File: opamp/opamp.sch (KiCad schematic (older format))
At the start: 7 parts, among them CON1 BARREL_JACK, CON2 BARREL_JACK, P1 PWR_IN, U1 OPAMP

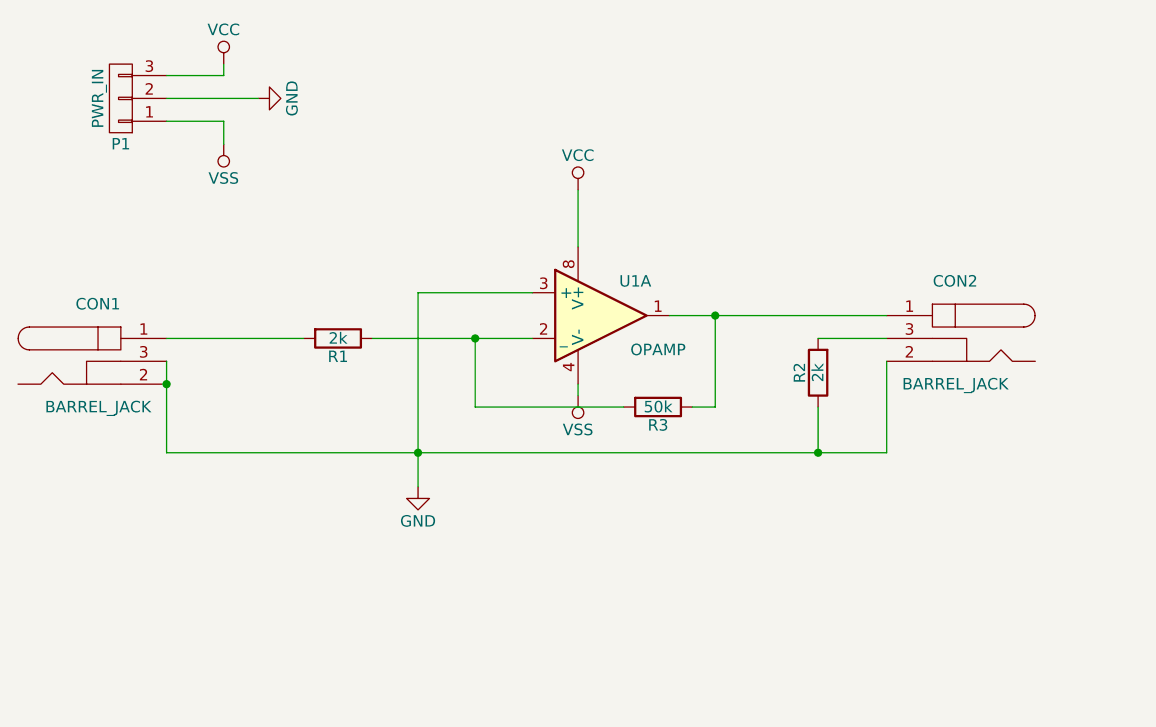
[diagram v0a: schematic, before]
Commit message: Added Simulation Circuits and POV board
Added a BJT characteristics simulation circuit
Add a Voltage Divider simulation circuit
Add an amplifier simulation circuit
Add a Nokia LCD breakout board
Add a POV LED MKL05Z board
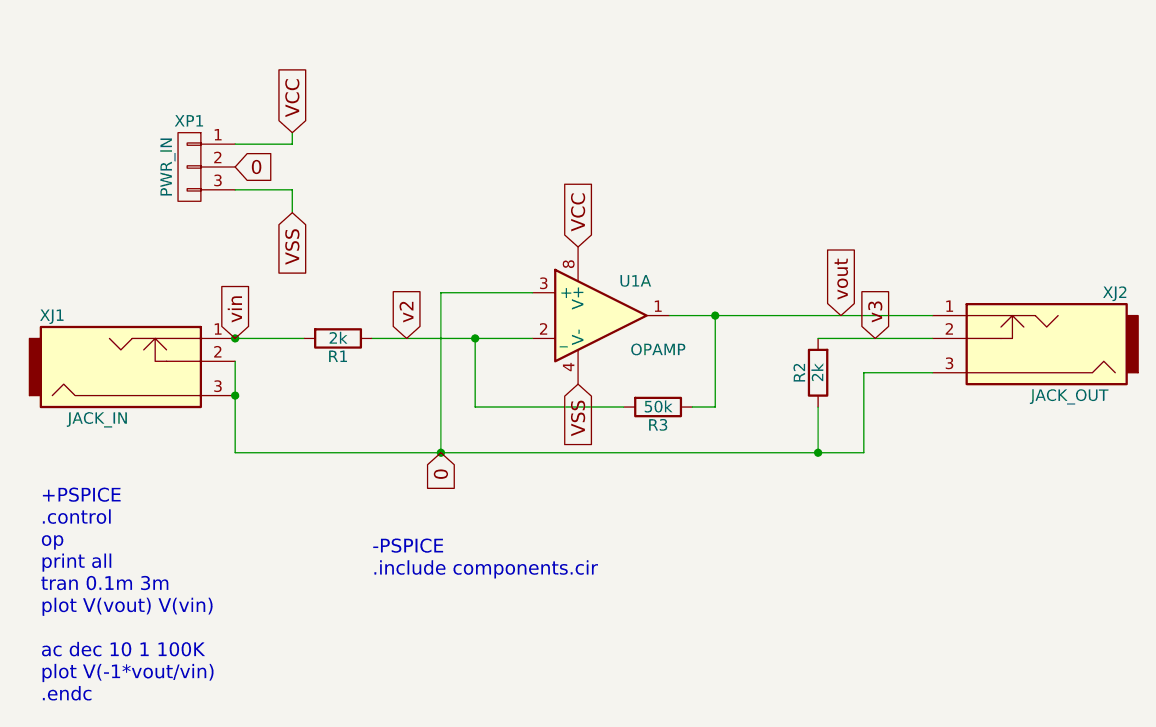
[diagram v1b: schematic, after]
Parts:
- removed CON1, CON2: BARREL_JACK, symbol BARREL_JACK
- added XJ1: JACK_IN, symbol JACK_2P
- added XJ2: JACK_OUT, symbol JACK_2P
- renumbered P1 to XP1
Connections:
- net VCC: now also XP1.1 (P1); no longer XP1.3 (P3)
- net VSS: now also XP1.3 (P3); no longer XP1.1 (P1)
- net v2: now reaches R1.1, R3.2, U1.2 (_)
- net vin: now reaches R1.2
- net vin: now also XJ1.1
- net v3: now reaches R2.2
- net v3: now also XJ2.2
- net vout: now reaches R3.1, U1.1
- net vout: now also XJ2.1
- net GND renamed 0
- net 0: now also XJ1.2, XJ1.3, XJ2.3
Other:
- note added: "+PSPICE\n.control\nop\nprint all\ntran 0.1m 3m\nplot V(vout) V(vin)\n\nac dec 10 1 100K\nplot V(-1*vout/vin)\n.endc"
- note added: "-PSPICE\n.include components.cir"
- moved on the sheet: XP1
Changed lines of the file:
@@
-$EndComp
-$Comp
-L VSS #PWR01
-U 1 1 57F76045
-P 5400 3200
-F 0 "#PWR01" H 5400 3050 50  0001 C CNN
-F 1 "VSS" H 5400 3350 50  0000 C CNN
-F 2 "" H 5400 3200 50  0000 C CNN
-F 3 "" H 5400 3200 50  0000 C CNN
-	1    5400 3200
-	-1   0    0    1
-$EndComp
-$Comp
-L BARREL_JACK CON1
-U 1 1 57F76321
-P 3300 3050
-F 0 "CON1" H 3300 3300 50  0000 C CNN
-F 1 "BARREL_JACK" H 3300 2850 50  0000 C CNN
-F 2 "" H 3300 3050 50  0000 C CNN
-F 3 "" H 3300 3050 50  0000 C CNN
-	1    3300 3050
-	1    0    0    -1
-$EndComp
-$Comp
-L BARREL_JACK CON2
-U 1 1 57F7634E
-P 7050 2950
-F 0 "CON2" H 7050 3200 50  0000 C CNN
-F 1 "BARREL_JACK" H 7050 2750 50  0000 C CNN
-F 2 "" H 7050 2950 50  0000 C CNN
-F 3 "" H 7050 2950 50  0000 C CNN
-	1    7050 2950
-	-1   0    0    -1
 $EndComp
 $Comp
@@
 $EndComp
 $Comp
-L GND #PWR02
-U 1 1 57F7696D
-P 4700 3600
-F 0 "#PWR02" H 4700 3350 50  0001 C CNN
-F 1 "GND" H 4700 3450 50  0000 C CNN
-F 2 "" H 4700 3600 50  0000 C CNN
-F 3 "" H 4700 3600 50  0000 C CNN
-	1    4700 3600
+L CONN_01X03 XP1
+U 1 1 57F76C49
+P 3700 2200
+F 0 "XP1" H 3700 2400 50  0000 C CNN
+F 1 "PWR_IN" V 3800 2200 50  0000 C CNN
+F 2 "" H 3700 2200 50  0000 C CNN
+F 3 "" H 3700 2200 50  0000 C CNN
+	1    3700 2200
+	-1   0    0    -1
+$EndComp
+$Comp
+L LM193 U1
+U 1 1 5820773C
+P 5500 2850
+F 0 "U1" H 5650 3000 50  0000 C CNN
+F 1 "OPAMP" H 5750 2700 50  0000 C CNN
+F 2 "" H 5500 2850 50  0000 C CNN
+F 3 "" H 5500 2850 50  0000 C CNN
+	1    5500 2850
 	1    0    0    -1
 $EndComp
+Text GLabel 4800 3450 3    60   Input ~ 0
+0
+Text GLabel 5400 3150 3    60   Input ~ 0
+VSS
+Text GLabel 4150 2400 3    60   Input ~ 0
+VSS
+Text Notes 3050 4550 0    60   ~ 0
++PSPICE\n.control\nop\nprint all\ntran 0.1m 3m\nplot V(vout) V(vin)\n\nac dec 10 1 100K\nplot V(-1*vout/vin)\n.endc
+Text GLabel 3900 2950 1    60   Input ~ 0
+vin
+Text GLabel 6550 2850 1    60   Input ~ 0
+vout
+Text GLabel 4650 2950 1    60   Input ~ 0
+v2
+Text GLabel 6700 2950 1    60   Input ~ 0
+v3
+Text GLabel 3900 2200 2    60   Input ~ 0
+0
 $Comp
-L CONN_01X03 P1
-U 1 1 57F76C49
-P 3400 1900
-F 0 "P1" H 3400 2100 50  0000 C CNN
-F 1 "PWR_IN" V 3500 1900 50  0000 C CNN
-F 2 "" H 3400 1900 50  0000 C CNN
-F 3 "" H 3400 1900 50  0000 C CNN
-	1    3400 1900
+L JACK_2P XJ1
+U 1 1 59346446
+P 3450 3050
+F 0 "XJ1" H 3100 2850 50  0000 C CNN
+F 1 "JACK_IN" H 3300 3300 50  0000 C CNN
+F 2 "" H 3450 3050 50  0001 C CNN
+F 3 "" H 3450 3050 50  0001 C CNN
+	1    3450 3050
+	1    0    0    1
+$EndComp
+$Comp
+L JACK_2P XJ2
+U 1 1 59346830
+P 7400 2950
+F 0 "XJ2" H 7050 2750 50  0000 C CNN
+F 1 "JACK_OUT" H 7250 3200 50  0000 C CNN
+F 2 "" H 7400 2950 50  0001 C CNN
+F 3 "" H 7400 2950 50  0001 C CNN
+	1    7400 2950
 	-1   0    0    1
 $EndComp
-$Comp
-L VCC #PWR03
-U 1 1 57F76CA4
-P 3850 1750
-F 0 "#PWR03" H 3850 1600 50  0001 C CNN
-F 1 "VCC" H 3850 1900 50  0000 C CNN
-F 2 "" H 3850 1750 50  0000 C CNN
-F 3 "" H 3850 1750 50  0000 C CNN
-	1    3850 1750
-	1    0    0    -1
-$EndComp
-$Comp
-L VSS #PWR04
-U 1 1 57F76CC6
-P 3850 2100
-F 0 "#PWR04" H 3850 1950 50  0001 C CNN
-F 1 "VSS" H 3850 2250 50  0000 C CNN
-F 2 "" H 3850 2100 50  0000 C CNN
-F 3 "" H 3850 2100 50  0000 C CNN
-	1    3850 2100
-	-1   0    0    1
-$EndComp
-$Comp
-L GND #PWR05
-U 1 1 57F76CE8
-P 4000 1900
-F 0 "#PWR05" H 4000 1650 50  0001 C CNN
-F 1 "GND" H 4000 1750 50  0000 C CNN
-F 2 "" H 4000 1900 50  0000 C CNN
-F 3 "" H 4000 1900 50  0000 C CNN
-	1    4000 1900
-	0    -1   -1   0
-$EndComp
-Wire Wire Line
-	5400 3150 5400 3200
-Wire Wire Line
-	3600 2950 4200 2950
 Wire Wire Line
 	4500 2950 5200 2950
 Wire Wire Line
-	5800 2850 6750 2850
+	5800 2850 6950 2850
 Wire Wire Line
-	6750 2950 6450 2950
-Wire Wire Line
-	6750 3450 6750 3050
-Wire Wire Line
-	3600 3450 6750 3450
+	6450 2950 6950 2950
 Wire Wire Line
 	6450 3450 6450 3250
-Wire Wire Line
-	3600 3050 3600 3450
-Connection ~ 6450 3450
-Connection ~ 3600 3150
 Wire Wire Line
 	5900 3250 6000 3250
@@
 Connection ~ 4950 2950
 Wire Wire Line
-	4700 2750 4700 3600
-Connection ~ 4700 3450
+	4150 2050 4150 2100
 Wire Wire Line
-	5200 2750 4700 2750
+	4150 2100 3900 2100
 Wire Wire Line
-	3850 1750 3850 1800
+	4150 2400 4150 2300
 Wire Wire Line
-	3850 1800 3600 1800
+	4150 2300 3900 2300
 Wire Wire Line
-	3600 1900 4000 1900
+	4800 3450 4800 2750
 Wire Wire Line
-	3850 2100 3850 2000
+	4800 2750 5200 2750
 Wire Wire Line
-	3850 2000 3600 2000
-$Comp
-L LM193 U1
-U 1 1 5820773C
-P 5500 2850
-F 0 "U1" H 5650 3000 50  0000 C CNN
-F 1 "OPAMP" H 5750 2700 50  0000 C CNN
-F 2 "" H 5500 2850 50  0000 C CNN
-F 3 "" H 5500 2850 50  0000 C CNN
-	1    5500 2850
-	1    0    0    -1
-$EndComp
-$Comp
-L VCC #PWR06
-U 1 1 5820919C
-P 5400 2300
-F 0 "#PWR06" H 5400 2150 50  0001 C CNN
-F 1 "VCC" H 5400 2450 50  0000 C CNN
-F 2 "" H 5400 2300 50  0000 C CNN
-F 3 "" H 5400 2300 50  0000 C CNN
-	1    5400 2300
-	1    0    0    -1
-$EndComp
+	6650 3450 6650 3100
 Wire Wire Line
-	5400 2300 5400 2550
+	6650 3100 6950 3100
+Connection ~ 3900 2950
+Wire Wire Line
+	3900 2950 4200 2950
+Wire Wire Line
+	3900 3050 3900 3450
+Connection ~ 3900 3200
+Wire Wire Line
+	3900 3450 6650 3450
+Connection ~ 4800 3450
+Connection ~ 6450 3450
+Text Notes 4500 4000 0    60   ~ 0
+-PSPICE\n.include components.cir
+Text GLabel 4150 2050 1    60   Input ~ 0
+VCC
+Text GLabel 5400 2550 1    60   Input ~ 0
+VCC
 $EndSCHEMATC

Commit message: Too many untracked changes: LCD boards update and switch to KiCAD version 5
Update the Nokia LCD breakout boards
Add more KiCAD simulation projects
Update most projects to KiCAD version 5
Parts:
- R1, R2, R3: symbol R -> opamp-rescue:R
- U1: symbol LM193 -> opamp-rescue:LM193
- XJ1, XJ2: symbol JACK_2P -> opamp-rescue:JACK_2P
- XP1: symbol CONN_01X03 -> opamp-rescue:CONN_01X03
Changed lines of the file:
@@
-EESchema Schematic File Version 2
-LIBS:power
-LIBS:device
-LIBS:transistors
-LIBS:conn
-LIBS:linear
-LIBS:regul
-LIBS:74xx
-LIBS:cmos4000
-LIBS:adc-dac
-LIBS:memory
-LIBS:xilinx
-LIBS:microcontrollers
-LIBS:dsp
-LIBS:microchip
-LIBS:analog_switches
-LIBS:motorola
-LIBS:texas
-LIBS:intel
-LIBS:audio
-LIBS:interface
-LIBS:digital-audio
-LIBS:philips
-LIBS:display
-LIBS:cypress
-LIBS:siliconi
-LIBS:opto
-LIBS:atmel
-LIBS:contrib
-LIBS:valves
+EESchema Schematic File Version 4
 LIBS:opamp-cache
-EELAYER 25 0
+EELAYER 30 0
 EELAYER END
 $Descr A4 11693 8268
@@
 $EndDescr
 $Comp
-L R R1
+L opamp-rescue:R R1
 U 1 1 57F75DA1
 P 4350 2950
@@
 $EndComp
 $Comp
-L R R2
+L opamp-rescue:R R2
 U 1 1 57F75DC0
 P 6450 3100
@@
 $EndComp
 $Comp
-L R R3
+L opamp-rescue:R R3
 U 1 1 57F767C6
 P 5750 3250
@@
 $EndComp
 $Comp
-L CONN_01X03 XP1
+L opamp-rescue:CONN_01X03 XP1
 U 1 1 57F76C49
 P 3700 2200
@@
 $EndComp
 $Comp
-L LM193 U1
+L opamp-rescue:LM193 U1
 U 1 1 5820773C
 P 5500 2850
@@
 Text GLabel 4150 2400 3    60   Input ~ 0
 VSS
-Text Notes 3050 4550 0    60   ~ 0
-+PSPICE\n.control\nop\nprint all\ntran 0.1m 3m\nplot V(vout) V(vin)\n\nac dec 10 1 100K\nplot V(-1*vout/vin)\n.endc
 Text GLabel 3900 2950 1    60   Input ~ 0
 vin
@@
 0
 $Comp
-L JACK_2P XJ1
+L opamp-rescue:JACK_2P XJ1
 U 1 1 59346446
 P 3450 3050
@@
 $EndComp
 $Comp
-L JACK_2P XJ2
+L opamp-rescue:JACK_2P XJ2
 U 1 1 59346830
 P 7400 2950
@@
 $EndComp
 Wire Wire Line
-	4500 2950 5200 2950
+	4500 2950 4950 2950
 Wire Wire Line
-	5800 2850 6950 2850
+	5800 2850 6000 2850
 Wire Wire Line
 	6450 2950 6950 2950
@@
 Wire Wire Line
 	6650 3100 6950 3100
-Connection ~ 3900 2950
 Wire Wire Line
 	3900 2950 4200 2950
 Wire Wire Line
-	3900 3050 3900 3450
+	3900 3050 3900 3200
 Connection ~ 3900 3200
 Wire Wire Line
-	3900 3450 6650 3450
+	3900 3450 4800 3450
 Connection ~ 4800 3450
 Connection ~ 6450 3450
@@
 Text GLabel 5400 2550 1    60   Input ~ 0
 VCC
+Wire Wire Line
+	6000 2850 6950 2850
+Wire Wire Line
+	4950 2950 5200 2950
+Wire Wire Line
+	3900 3200 3900 3450
+Wire Wire Line
+	4800 3450 6450 3450
+Wire Wire Line
+	6450 3450 6650 3450
+Text Notes 3050 4550 0    60   ~ 0
++PSPICE\n.control\nop\nprint all\ntran 0.1m 3m\nplot V(vout) V(vin)\n\nac dec 10 1 100K\nplot V(-1*vout/vin)\n.endc
 $EndSCHEMATC
